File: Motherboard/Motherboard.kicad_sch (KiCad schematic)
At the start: 6 parts

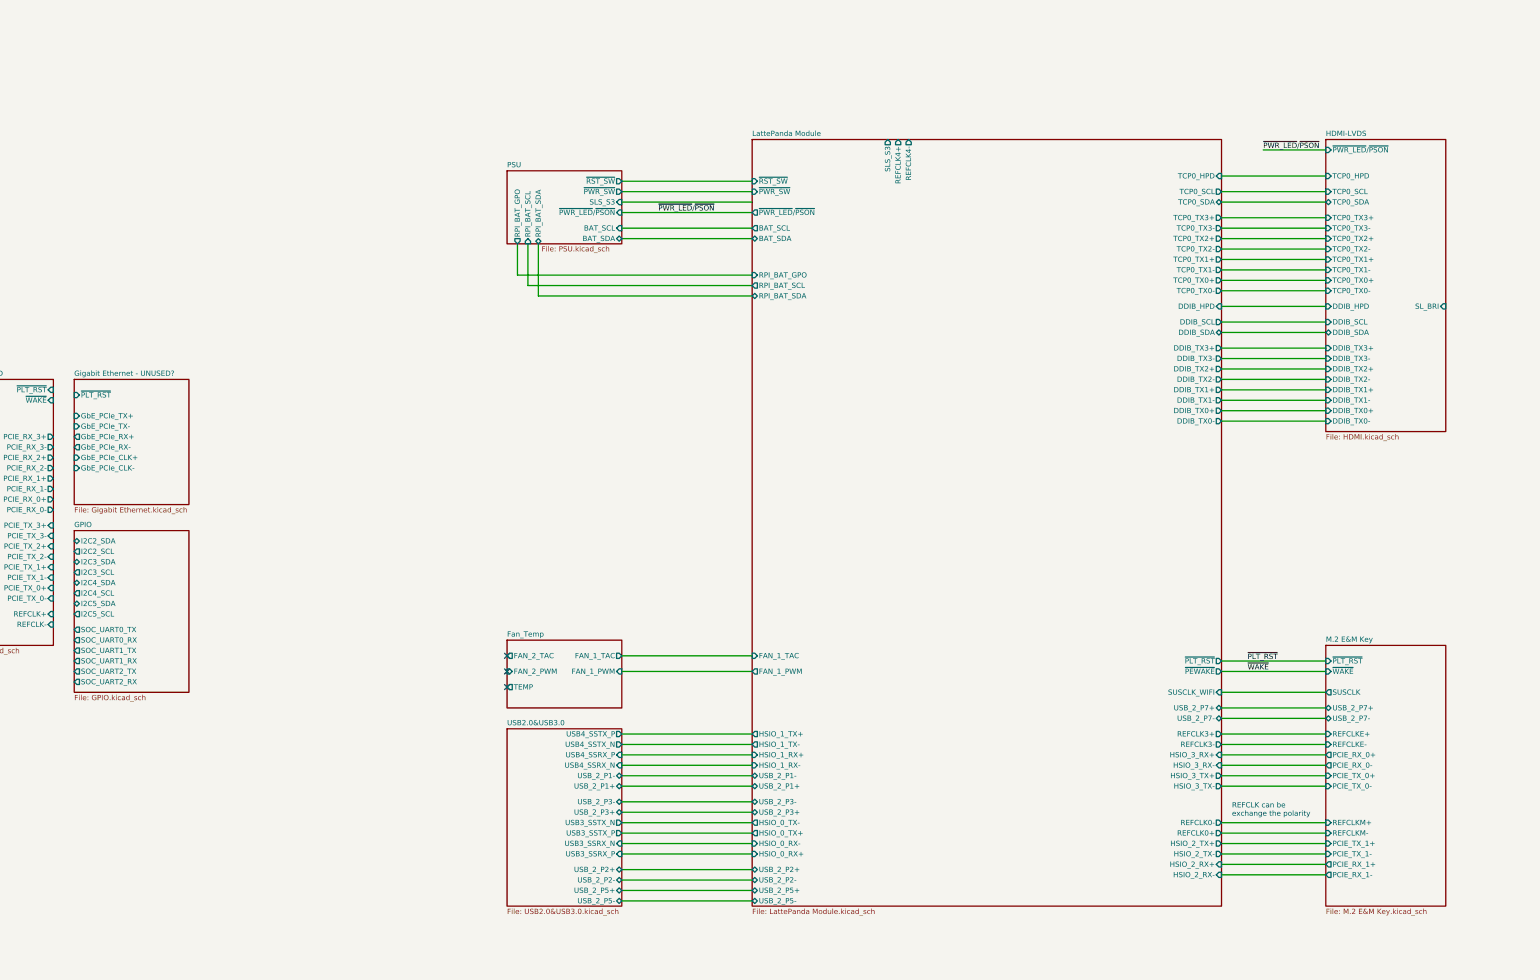
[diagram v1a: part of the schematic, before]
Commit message: Added RP2040 MCU, Handles all External IO Systems (Except Audio), WIP.
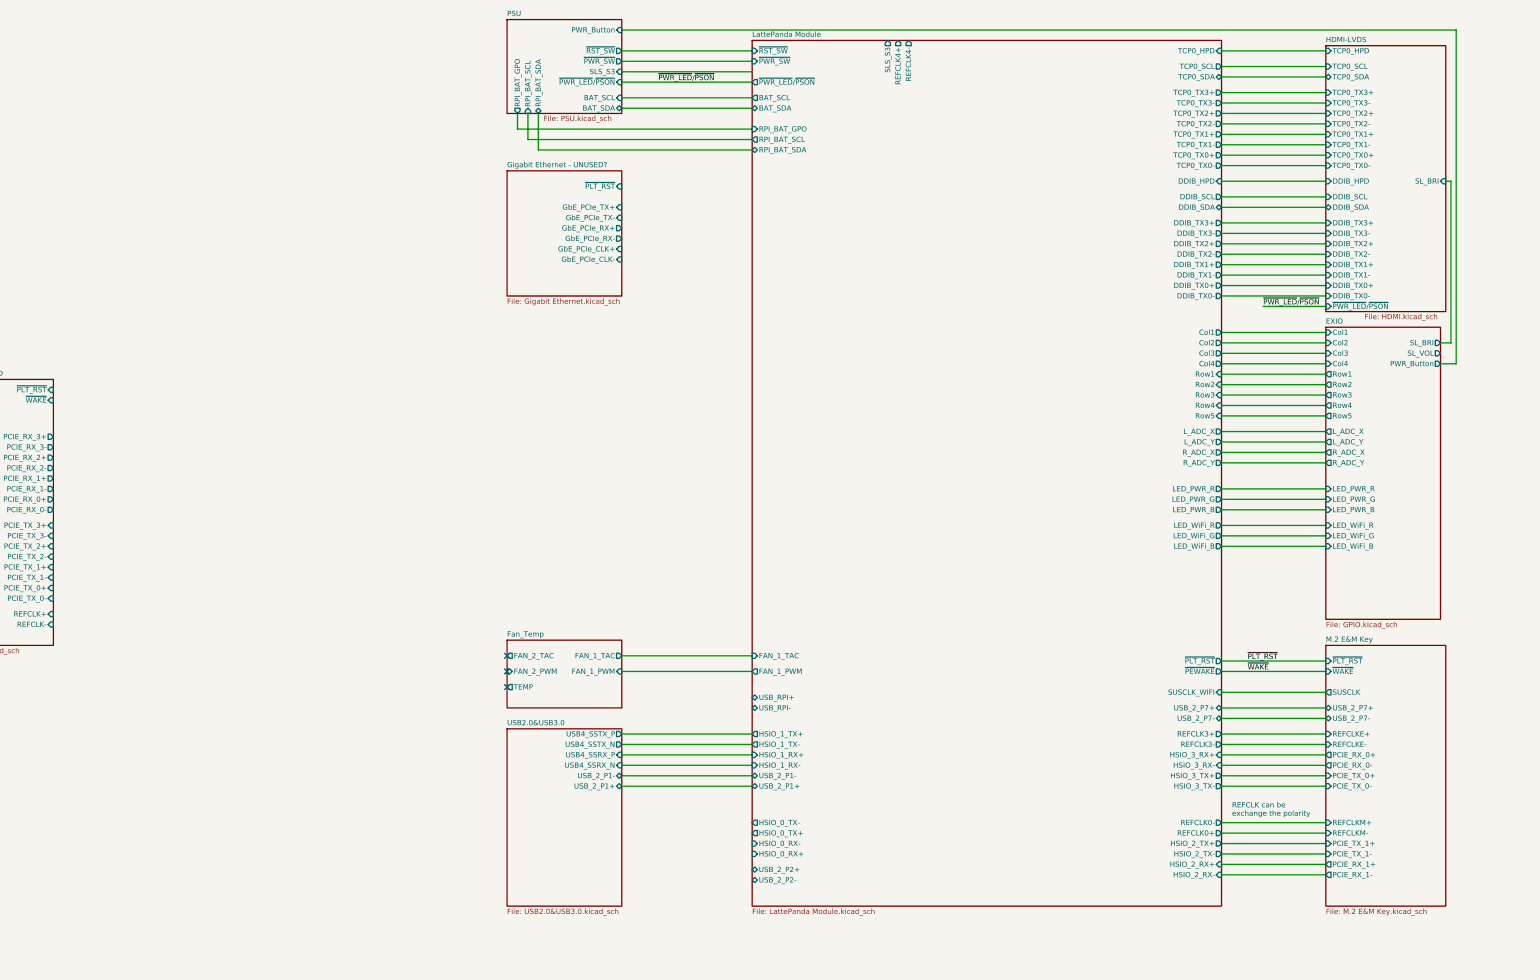
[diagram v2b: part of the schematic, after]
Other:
- sheet GPIO renamed EXIO
- sheet EXIO ports: added Col1, Col2, Col3, Col4, LED_PWR_B, LED_PWR_G, LED_PWR_R, LED_WiFi_B, LED_WiFi_G, LED_WiFi_R, L_ADC_X, L_ADC_Y, PWR_Button, R_ADC_X, R_ADC_Y, Row1, Row2, Row3, Row4, Row5, SL_BRI, SL_VOL; removed I2C2_SCL, I2C2_SDA, I2C3_SCL, I2C3_SDA, I2C4_SCL, I2C4_SDA, I2C5_SCL, I2C5_SDA, SOC_UART0_RX, SOC_UART0_TX, SOC_UART1_RX, SOC_UART1_TX, SOC_UART2_RX, SOC_UART2_TX
- sheet LattePanda Module ports: added Col1, Col2, Col3, Col4, LED_PWR_B, LED_PWR_G, LED_PWR_R, LED_WiFi_B, LED_WiFi_G, LED_WiFi_R, L_ADC_X, L_ADC_Y, R_ADC_X, R_ADC_Y, Row1, Row2, Row3, Row4, Row5, USB_RPI+, USB_RPI-; removed USB_2_P3+, USB_2_P3-, USB_2_P5+, USB_2_P5-
- sheet PSU ports: added PWR_Button; removed none
- sheet USB2.0&USB3.0 ports: added none; removed USB3_SSRX_N, USB3_SSRX_P, USB3_SSTX_N, USB3_SSTX_P, USB_2_P2+, USB_2_P2-, USB_2_P3+, USB_2_P3-, USB_2_P5+, USB_2_P5-

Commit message: Motherboard Complete (aside from parts-BOM associations)
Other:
- removed sheet Gigabit Ethernet - UNUSED?
- removed sheet PCIe x4 - UNUSED
- sheet LattePanda Module ports: added RPI_BAT_STAT, RPI_SLI_VOL, USB_2_P3+, USB_2_P3-, WiFi_M2E_LED; removed REFCLK4+, REFCLK4-, USB_RPI+, USB_RPI-
- sheet M.2 E&M Key ports: added RPi_WiFi_M2E; removed none
- sheet PSU ports: added BAT_STAT; removed none
- sheet USB2.0&USB3.0 ports: added USB3_SSRX_N, USB3_SSRX_P, USB3_SSTX_N, USB3_SSTX_P, USB_2_P2+, USB_2_P2-, USB_2_P3+, USB_2_P3-; removed none

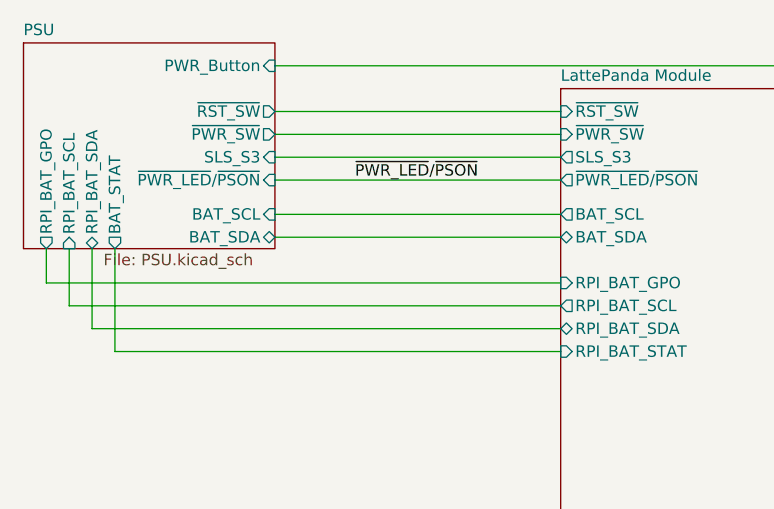
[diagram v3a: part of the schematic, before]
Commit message: Switched Screens to use RGB interface, ADV7613 -> ADV7611. Changes WIP
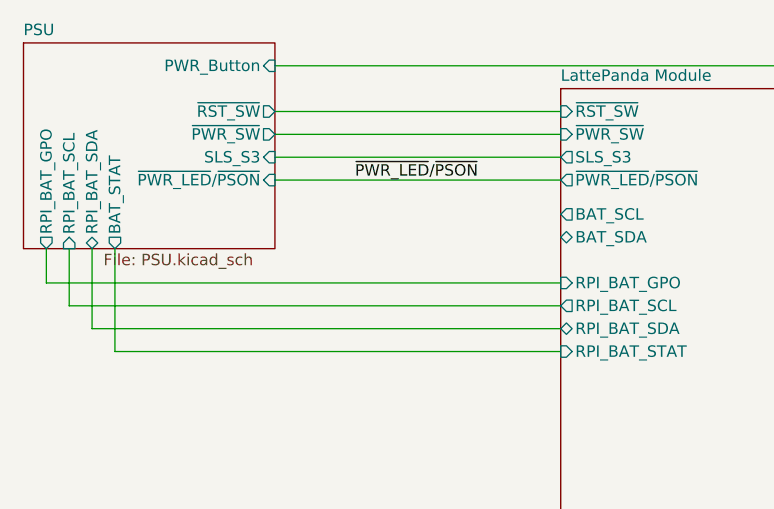
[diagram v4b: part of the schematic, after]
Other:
- sheet PSU ports: added none; removed BAT_SCL, BAT_SDA
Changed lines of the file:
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@@
 	(wire
 		(pts
-			(xy 195.58 88.9) (xy 227.33 88.9)
-		)
-		(stroke
-			(width 0)
-			(type default)
-		)
-	)
-	(wire
-		(pts
 			(xy 195.58 276.86) (xy 227.33 276.86)
 		)
@@
 	(wire
 		(pts
-			(xy 195.58 86.36) (xy 227.33 86.36)
-		)
-		(stroke
-			(width 0)
-			(type default)
-		)
-	)
-	(wire
-		(pts
 			(xy 341.63 81.28) (xy 367.03 81.28)
 		)
@@
 			(effects
 				(font
-					(size 1.27 1.27)
-				)
-				(justify right)
-			)
-		)
-		(pin "BAT_SDA" bidirectional
-			(at 195.58 88.9 0)
-			(effects
-				(font
-					(size 1.27 1.27)
-				)
-				(justify right)
-			)
-		)
-		(pin "BAT_SCL" input
-			(at 195.58 86.36 0)
-			(effects
-				(font

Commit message: Switched HDMI DBUG and TCP0 back, added I2C Protection circuits, and a lot more random changes/updates/progress
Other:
- sheet HDMI-LVDS ports: added DBUG_HPD, DBUG_SCL, DBUG_SDA, DBUG_TX0+, DBUG_TX0-, DBUG_TX1+, DBUG_TX1-, DBUG_TX2+, DBUG_TX2-, DBUG_TX3+, DBUG_TX3-, DDIB_ADV_SCL, DDIB_ADV_SDA, DDIB_INT, TCP0_ADV_SCL, TCP0_ADV_SDA, TCP0_INT; removed none
- sheet LattePanda Module ports: added DBUG_HPD, DBUG_SCL, DBUG_SDA, DBUG_TX0+, DBUG_TX0-, DBUG_TX1+, DBUG_TX1-, DBUG_TX2+, DBUG_TX2-, DBUG_TX3+, DBUG_TX3-, DDIB_ADV_SCL, DDIB_ADV_SDA, TCP0_ADV_SCL, TCP0_ADV_SDA; removed BAT_SCL, BAT_SDA

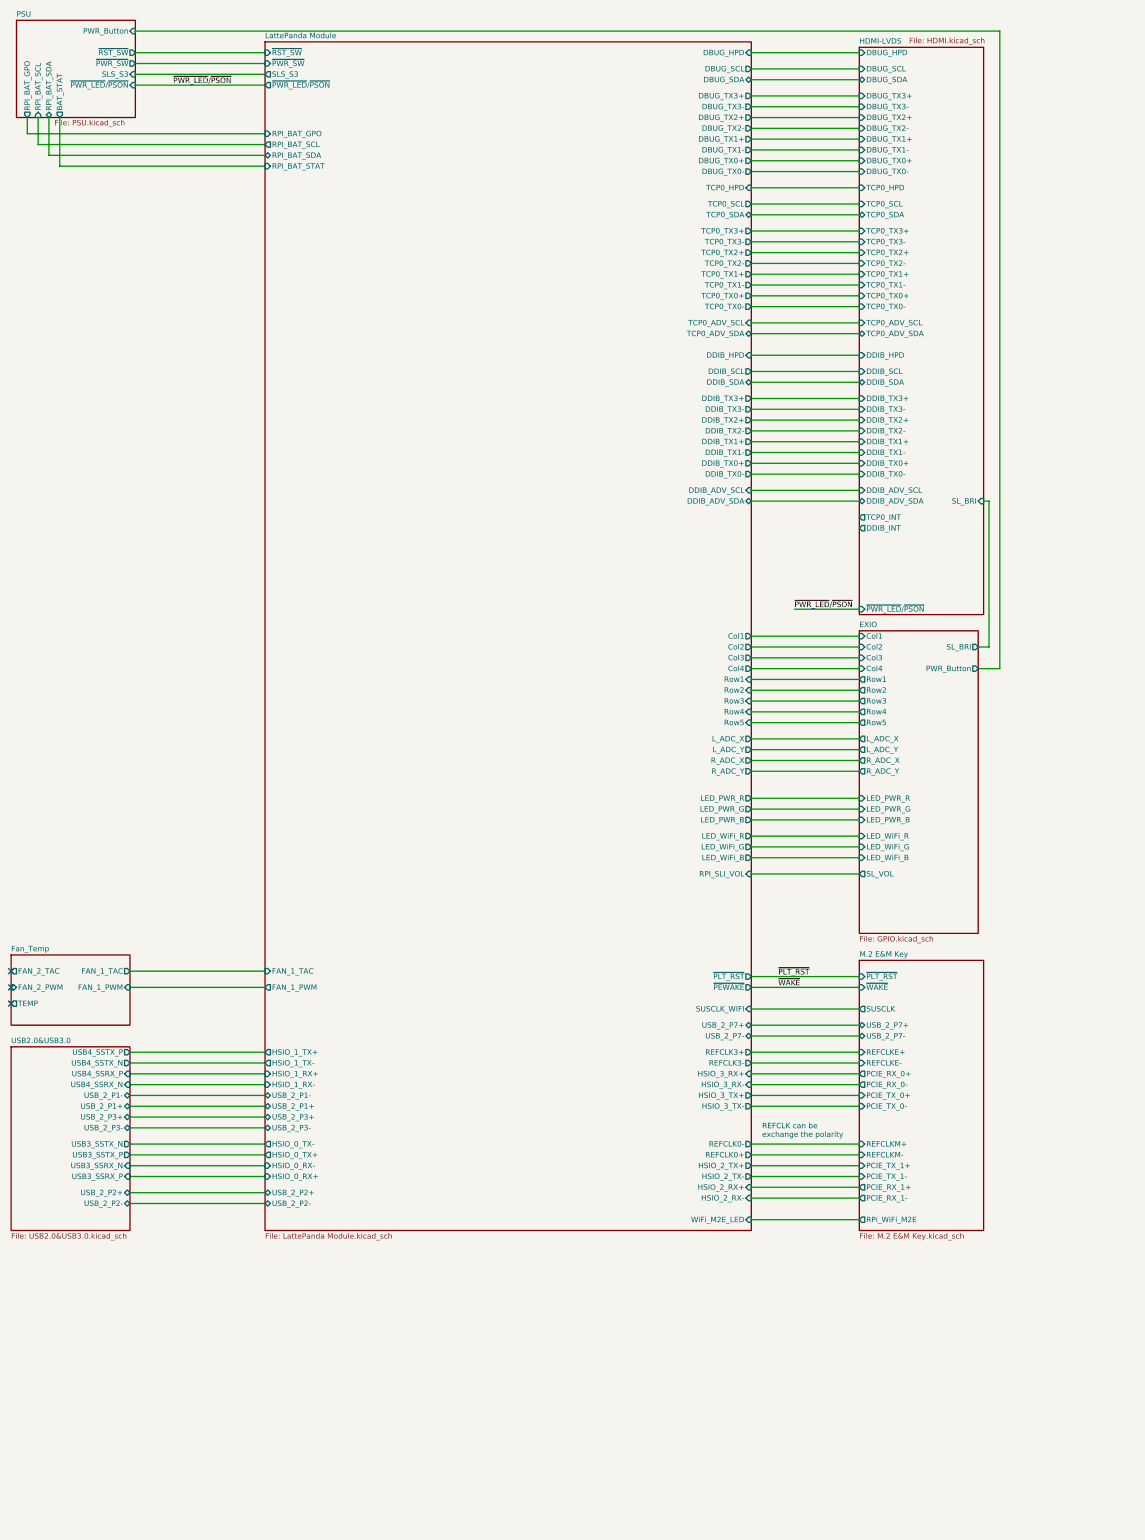
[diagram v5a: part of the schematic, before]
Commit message: Partial wiring of power path and top screen
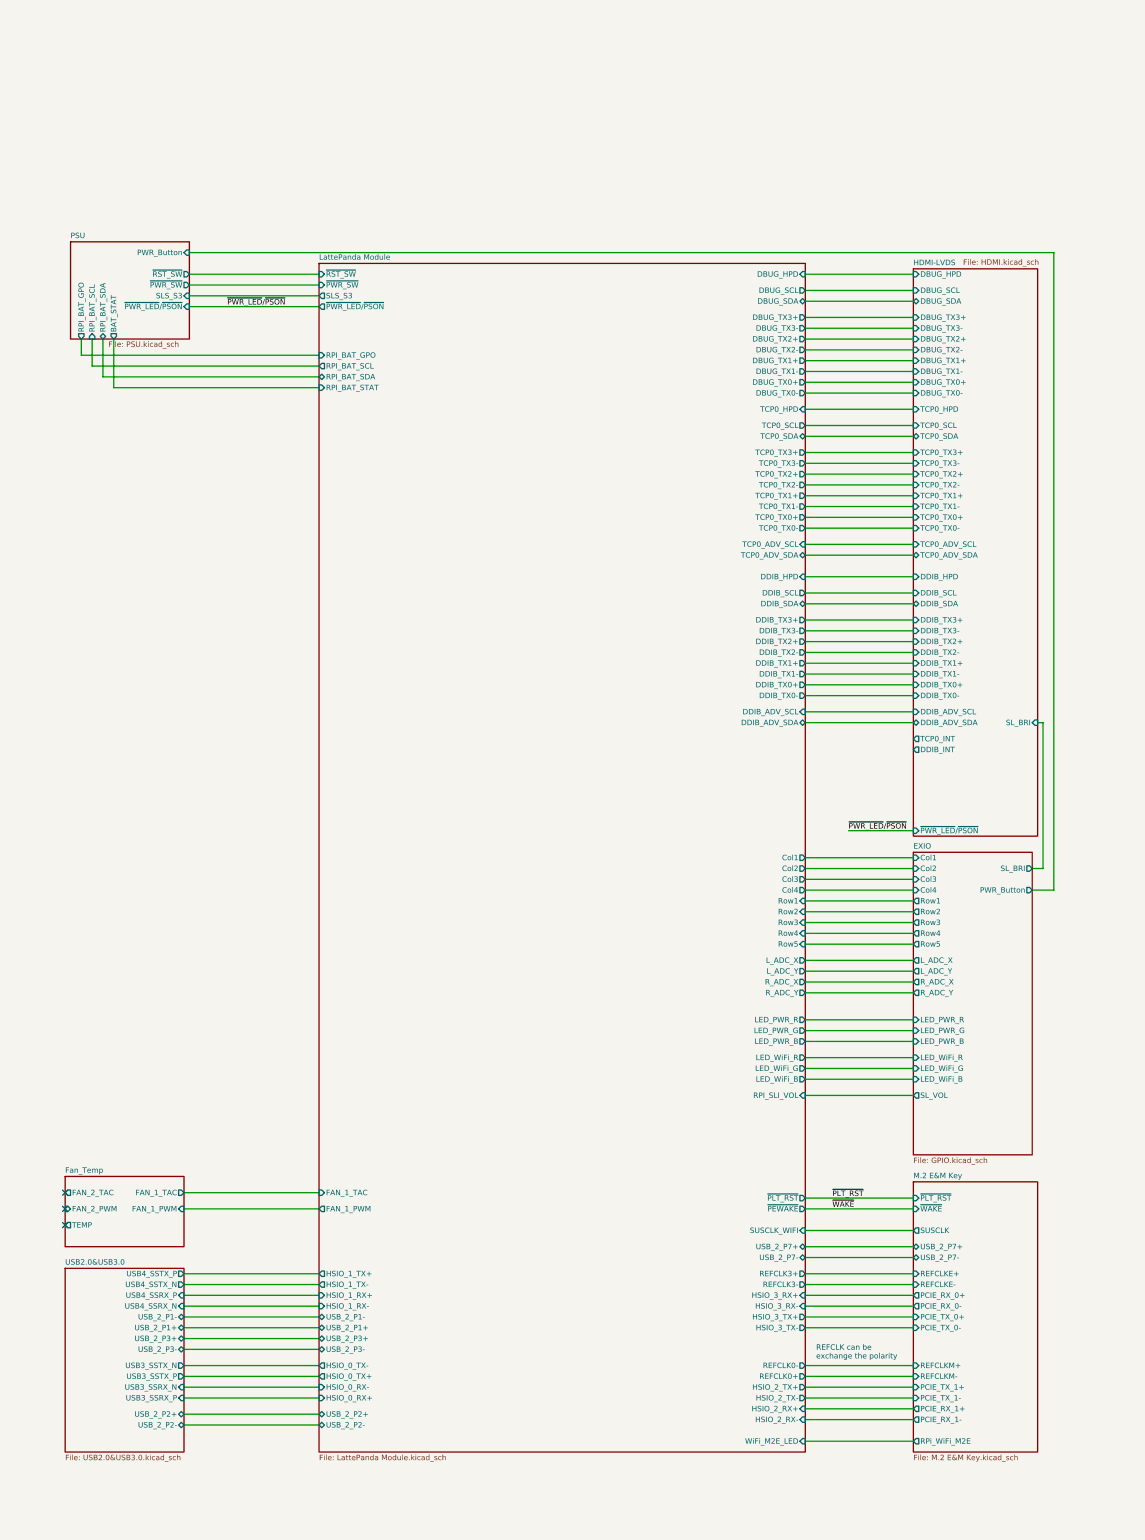
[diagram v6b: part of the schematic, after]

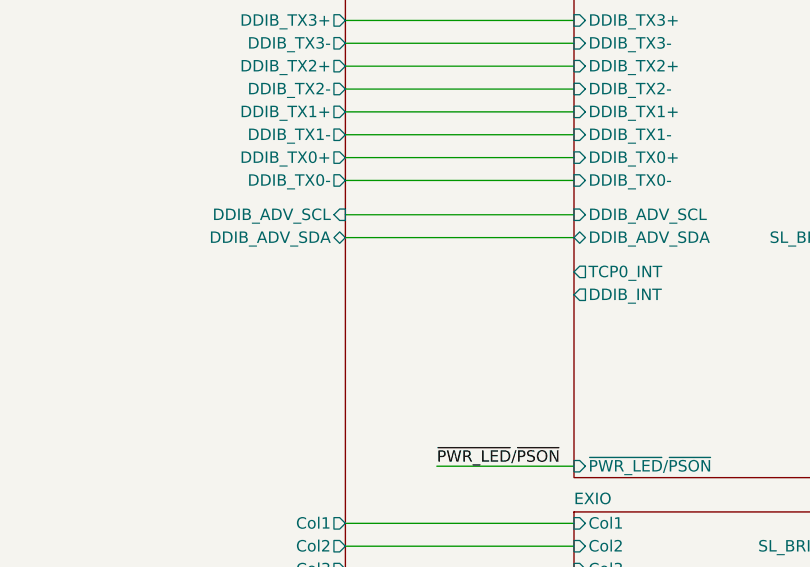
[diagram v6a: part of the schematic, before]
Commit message: HDMI-TCP0 Screen wired!
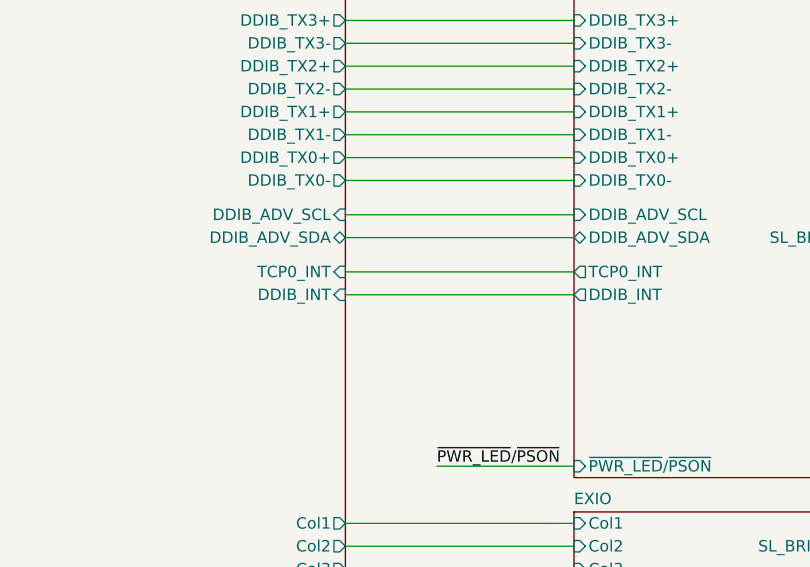
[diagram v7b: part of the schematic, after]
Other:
- sheet LattePanda Module ports: added DDIB_INT, TCP0_INT; removed none
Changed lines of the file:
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@@
 	(wire
 		(pts
+			(xy 354.33 170.18) (xy 379.73 170.18)
+		)
+		(stroke
+			(width 0)
+			(type default)
+		)
+	)
+	(wire
+		(pts
 			(xy 186.69 80.01) (xy 186.69 73.66)
 		)
@@
 	(wire
 		(pts
+			(xy 354.33 167.64) (xy 379.73 167.64)
+		)
+		(stroke
+			(width 0)
+			(type default)
+		)
+	)
+	(wire
+		(pts
 			(xy 354.33 81.28) (xy 379.73 81.28)
 		)
@@
 			(effects
 				(font
+					(size 1.27 1.27)
+				)
+				(justify right)
+			)
+		)
+		(pin "DDIB_INT" input
+			(at 354.33 170.18 0)
+			(effects
+				(font
+					(size 1.27 1.27)
+				)
+				(justify right)
+			)
+		)
+		(pin "TCP0_INT" input
+			(at 354.33 167.64 0)
+			(effects
+				(font
